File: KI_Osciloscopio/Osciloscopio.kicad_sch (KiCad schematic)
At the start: 40 parts, among them J1 Barrel Jack, U1 MCP6004, U2 74HC4051, U3 LM7805, U4 LM1117-3.3

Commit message: Esquematico terminado
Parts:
- removed U3: LM7805, Package_TO_SOT_THT:TO-220-3_Vertical, symbol Regulator_Linear:LM7805_TO220
- removed V1: VALUE, symbol pspice:VSOURCE
- added CN10: Conn_01x02_Female, symbol Connector:Conn_01x02_Female
- added CN5: Conn_01x10_Male, symbol Connector:Conn_01x10_Male
- added CN6, CN9: Conn_01x08_Male, symbol Connector:Conn_01x08_Male
- added CN8: Conn_01x06_Male, symbol Connector:Conn_01x06_Male
- added J1: Conn_Coaxial, symbol Connector:Conn_Coaxial
- added J2: USB_B, symbol Connector:USB_B
- added J2: OLED 128x64, symbol Connector:Conn_01x04_Male
- added JP1: Jumper_2_Open, symbol Jumper:Jumper_2_Open
- added U3: LM2940CT-5.0/NOPB, TO_SOT_Packages_THT:TO-220_Vertical, symbol AOI-LM2940CT:LM2940CT-5.0/NOPB
- added U5: M95128, Package_SO:SOIC-8_3.9x4.9mm_P1.27mm, symbol Memory_EEPROM:M95256-WMN6P
- C1: value 100uF -> 22uF
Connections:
- net 3.3V: now also CN6.5 (Pin_5), J2.3 (Pin_3), U5.3 (~{W}), U5.7 (~{HOLD}), U5.8 (VCC)
- net A0: now also CN8.1 (Pin_1)
- net A1: now also CN8.2 (Pin_2)
- net Earth: now also U3.2 (GND)
- net GNDREF: now also CN5.7 (Pin_7), CN6.2 (Pin_2), CN6.3 (Pin_3), J1.2 (Ext), J2.4 (GND), J2.4 (Pin_4), J2.5 (Shield), U5.4 (VSS)
- net VCC: now also CN6.4 (Pin_4), JP1.1 (A), U3.3 (OUT)
- net VDD: now also U3.1 (IN)
- net at C1.2: now also J1.1 (In)
- net D06 renamed D9
- net D9: now also CN5.2 (Pin_2)
- net D09 renamed D6
- net D6: now also CN9.7 (Pin_7)
- net D11 renamed D8
- net D8: now also CN5.1 (Pin_1)
- net D12 renamed D7
- net D7: now also CN9.8 (Pin_8)
- new net A2: CN8.3 (Pin_3)
- new net A3: CN8.4 (Pin_4)
- new net A4: CN8.5 (Pin_5)
- new net A5: CN8.6 (Pin_6)
- new net AVDD: CN5.8 (Pin_8)
- new net CS: CN5.3 (Pin_3), U5.1 (~{S})
- new net D+: CN10.1 (Pin_1), J2.3 (D+)
- new net D-: CN10.2 (Pin_2), J2.2 (D-)
- new net D0: CN9.1 (Pin_1)
- new net D1: CN9.2 (Pin_2)
- new net D2: CN9.3 (Pin_3)
- new net D3: CN9.4 (Pin_4)
- new net D4: CN9.5 (Pin_5)
- new net D5: CN9.6 (Pin_6)
- new net IOREF: CN6.7 (Pin_7)
- new net MISO: CN5.5 (Pin_5), U5.2 (Q)
- new net MOSI: CN5.4 (Pin_4), U5.5 (D)
- new net NRST: CN6.6 (Pin_6)
- new net SCK: CN5.6 (Pin_6), U5.6 (C)
- new net SCL: CN5.10 (Pin_10), J2.2 (Pin_2)
- new net SDA: CN5.9 (Pin_9), J2.1 (Pin_1)
- new net VBUS: J2.1 (VBUS)
- new net VIN: CN6.1 (Pin_1), JP1.2 (B)
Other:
- note added: "ALIMENTACION"
- note added: "STM32F401RE"
- moved on the sheet: C1, C11, C12, C2, C3, C4, C5, C6, C7, C8, C9, D3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

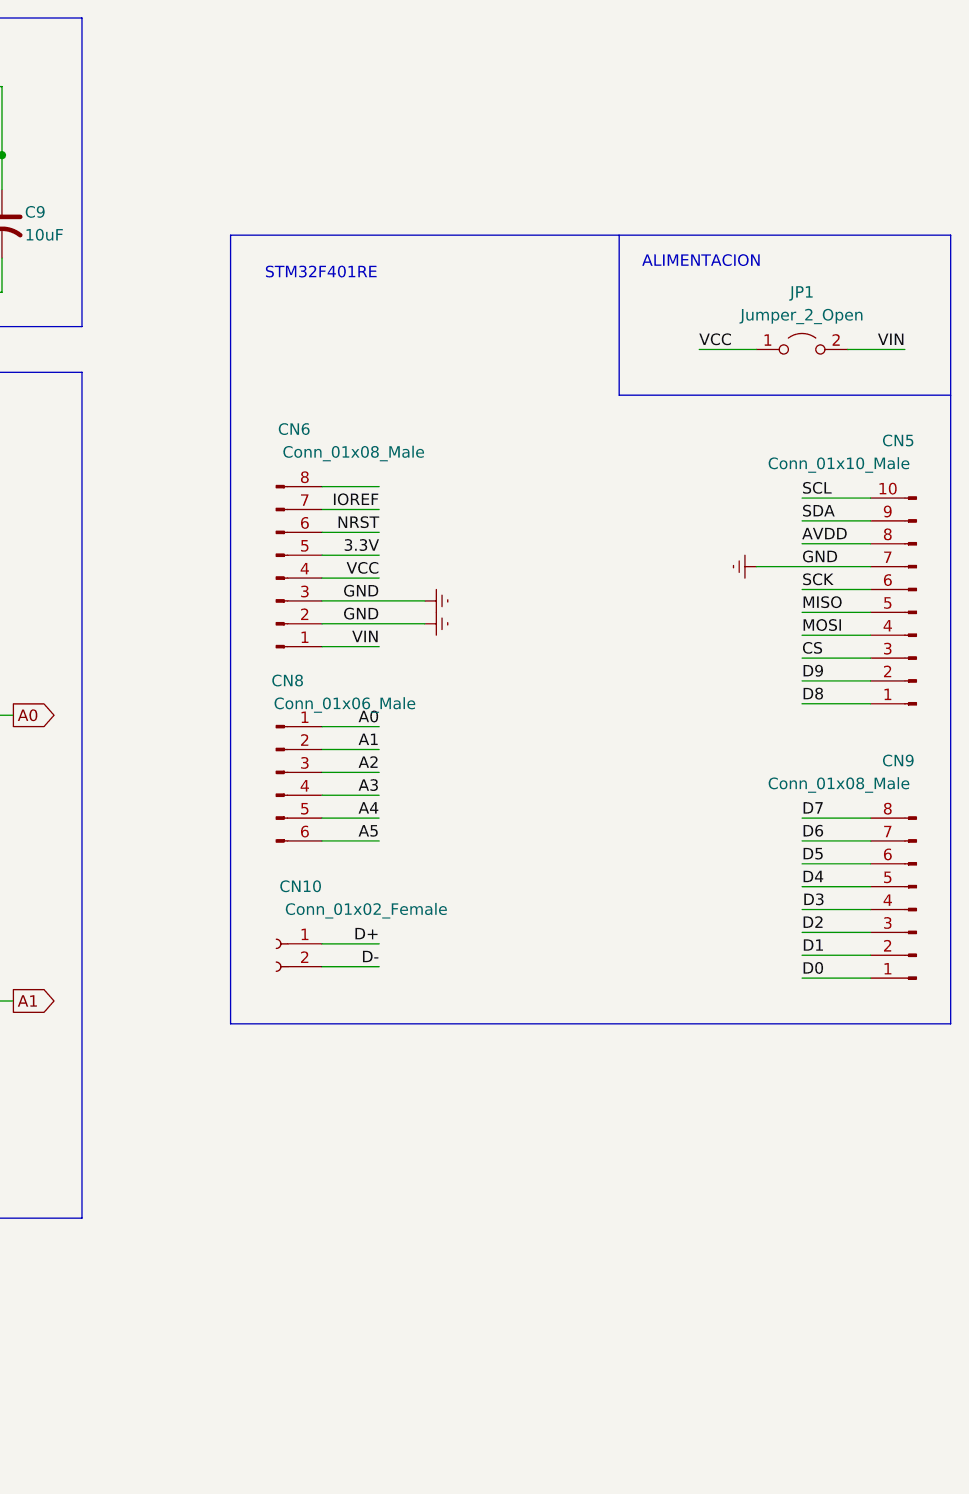
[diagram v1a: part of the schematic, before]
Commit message: Agregue Pines para ST en la placa
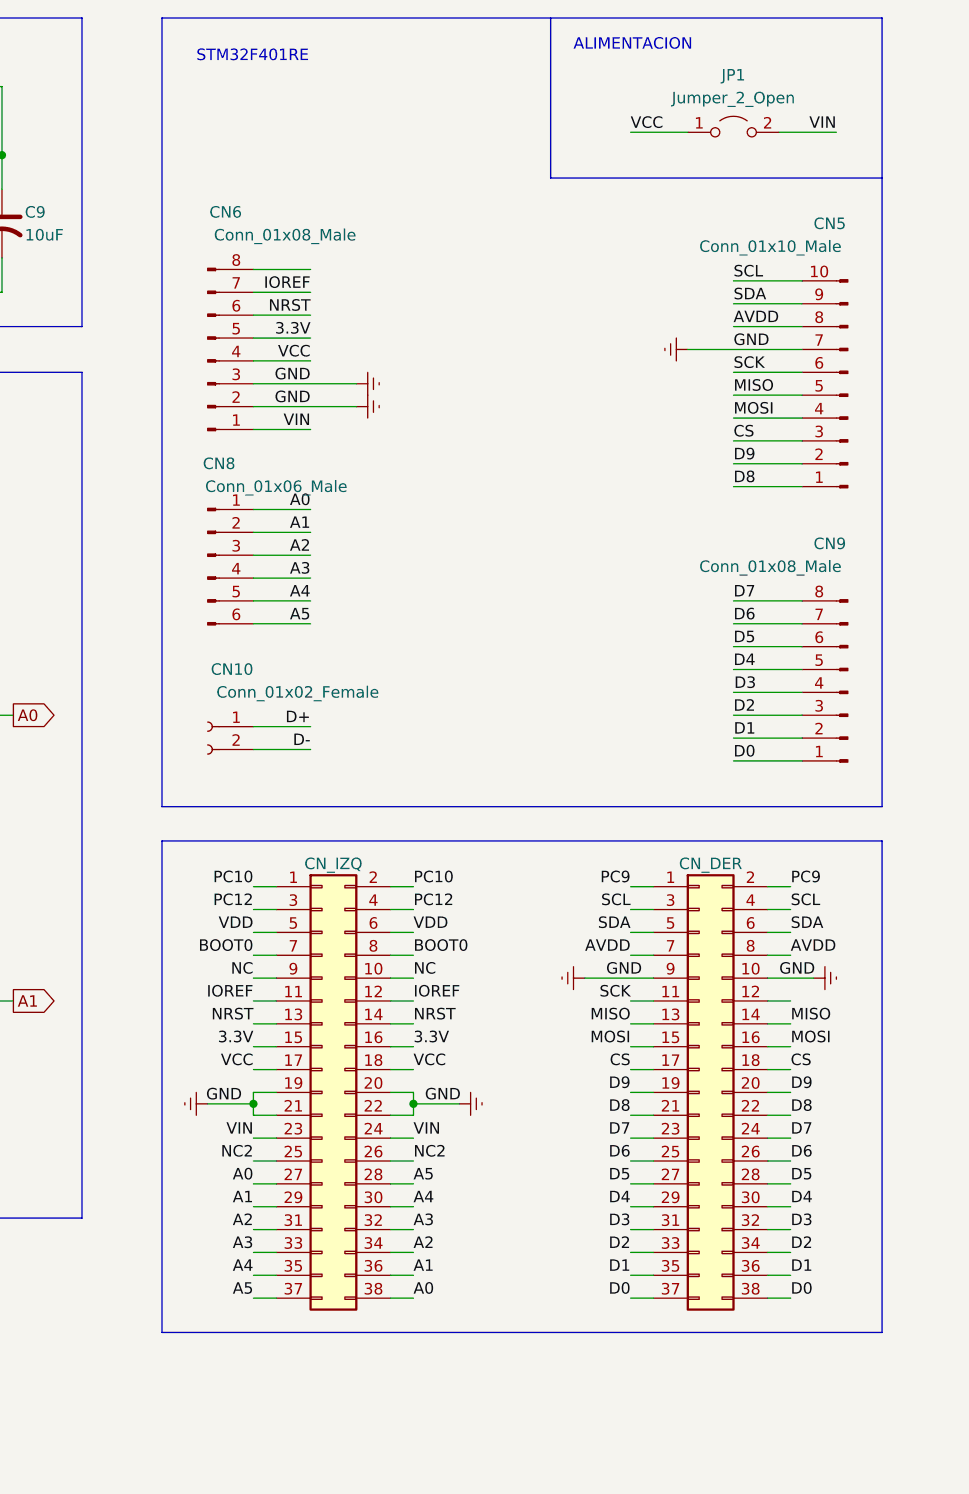
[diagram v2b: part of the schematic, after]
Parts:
- added CN_DER, CN_IZQ: Conn_02x19_Odd_Even, symbol Connector_Generic:Conn_02x19_Odd_Even
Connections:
- net GNDREF is gone; now on net Earth: C11.1, CN5.7 (Pin_7), CN6.2 (Pin_2), CN6.3 (Pin_3), J1.2 (Ext), J2.4 (GND), J2.4 (Pin_4), J2.5 (Shield), R12.2, R17.2, R20.2, U2.7 (VEE), U2.8 (GND), U5.4 (VSS)
- net 3.3V: now also CN_IZQ.15 (Pin_15), CN_IZQ.16 (Pin_16)
- net A0: now also CN_IZQ.27 (Pin_27), CN_IZQ.38 (Pin_38)
- net A1: now also CN_IZQ.29 (Pin_29), CN_IZQ.36 (Pin_36)
- net A2: now also CN_IZQ.31 (Pin_31), CN_IZQ.34 (Pin_34)
- net A3: now also CN_IZQ.32 (Pin_32), CN_IZQ.33 (Pin_33)
- net A4: now also CN_IZQ.30 (Pin_30), CN_IZQ.35 (Pin_35)
- net A5: now also CN_IZQ.28 (Pin_28), CN_IZQ.37 (Pin_37)
- net AVDD: now also CN_DER.7 (Pin_7), CN_DER.8 (Pin_8)
- net CS: now also CN_DER.17 (Pin_17), CN_DER.18 (Pin_18)
- net D0: now also CN_DER.37 (Pin_37), CN_DER.38 (Pin_38)
- net D1: now also CN_DER.35 (Pin_35), CN_DER.36 (Pin_36)
- net D2: now also CN_DER.33 (Pin_33), CN_DER.34 (Pin_34)
- net D3: now also CN_DER.31 (Pin_31), CN_DER.32 (Pin_32)
- net D4: now also CN_DER.29 (Pin_29), CN_DER.30 (Pin_30)
- net D5: now also CN_DER.27 (Pin_27), CN_DER.28 (Pin_28)
- net D6: now also CN_DER.25 (Pin_25), CN_DER.26 (Pin_26)
- net D7: now also CN_DER.23 (Pin_23), CN_DER.24 (Pin_24)
- net D8: now also CN_DER.21 (Pin_21), CN_DER.22 (Pin_22)
- net D9: now also CN_DER.19 (Pin_19), CN_DER.20 (Pin_20)
- net Earth: now also CN_DER.10 (Pin_10), CN_DER.9 (Pin_9), CN_IZQ.19 (Pin_19), CN_IZQ.20 (Pin_20), CN_IZQ.21 (Pin_21), CN_IZQ.22 (Pin_22)
- net IOREF: now also CN_IZQ.11 (Pin_11), CN_IZQ.12 (Pin_12)
- net MISO: now also CN_DER.13 (Pin_13), CN_DER.14 (Pin_14)
- net MOSI: now also CN_DER.15 (Pin_15), CN_DER.16 (Pin_16)
- net NRST: now also CN_IZQ.13 (Pin_13), CN_IZQ.14 (Pin_14)
- net SCK: now also CN_DER.11 (Pin_11)
- net SCL: now also CN_DER.3 (Pin_3), CN_DER.4 (Pin_4)
- net SDA: now also CN_DER.5 (Pin_5), CN_DER.6 (Pin_6)
- net VCC: now also CN_IZQ.17 (Pin_17), CN_IZQ.18 (Pin_18)
- net VDD: now also CN_IZQ.5 (Pin_5), CN_IZQ.6 (Pin_6)
- net VIN: now also CN_IZQ.23 (Pin_23), CN_IZQ.24 (Pin_24)
- new net BOOT0: CN_IZQ.7 (Pin_7), CN_IZQ.8 (Pin_8)
- new net NC: CN_IZQ.10 (Pin_10), CN_IZQ.9 (Pin_9)
- new net NC2: CN_IZQ.25 (Pin_25), CN_IZQ.26 (Pin_26)
- new net PC10: CN_IZQ.1 (Pin_1), CN_IZQ.2 (Pin_2)
- new net PC12: CN_IZQ.3 (Pin_3), CN_IZQ.4 (Pin_4)
- new net PC9: CN_DER.1 (Pin_1), CN_DER.2 (Pin_2)
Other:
- moved on the sheet: CN10, CN5, CN6, CN8, CN9, JP1

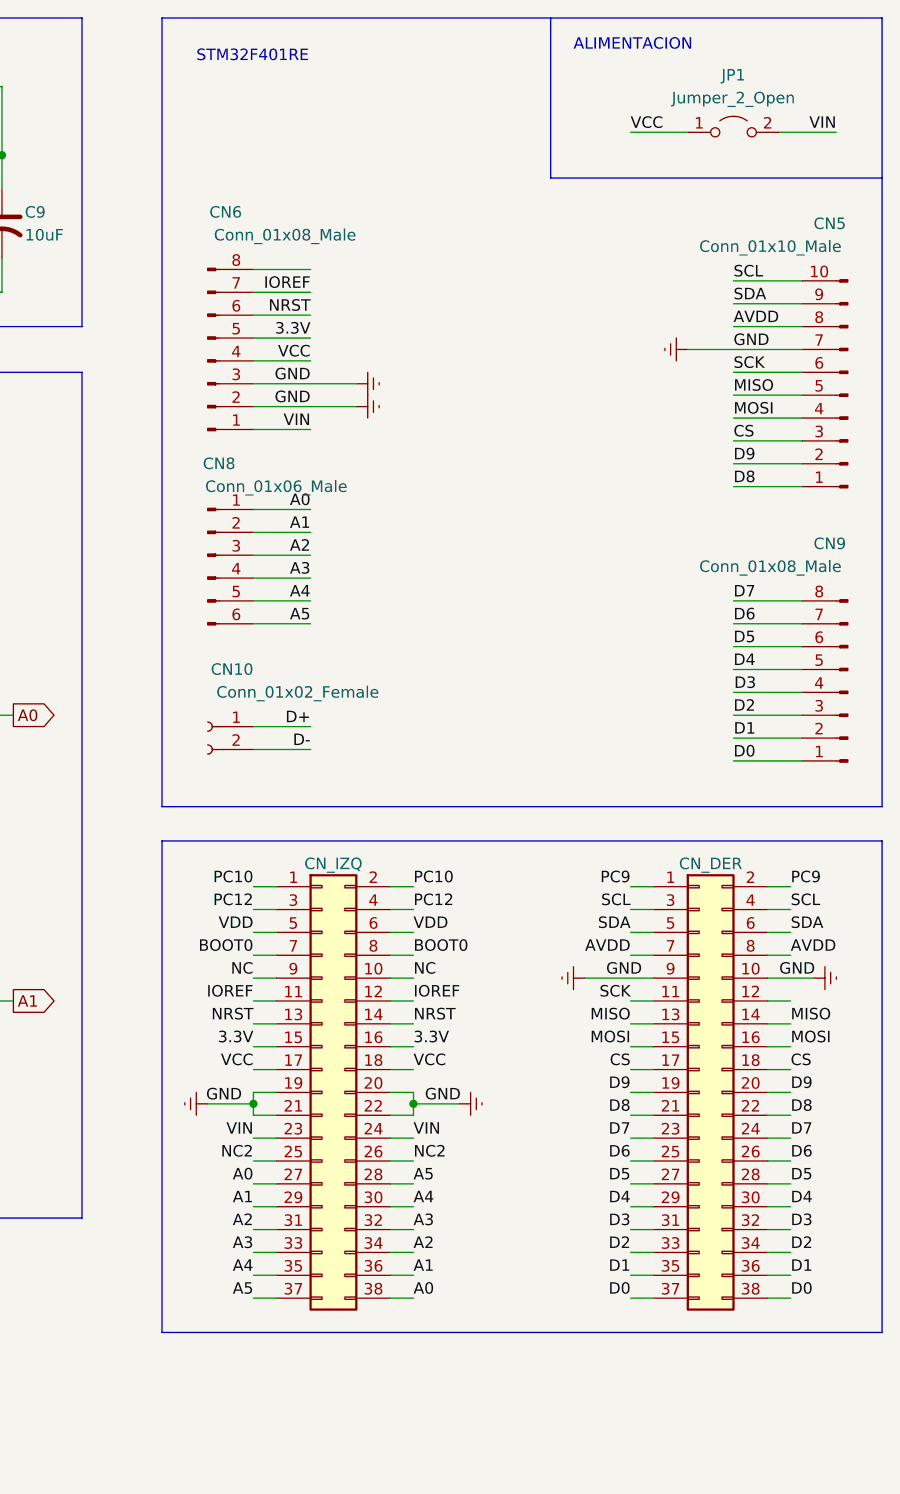
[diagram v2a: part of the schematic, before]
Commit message: Agregue algunos footprints
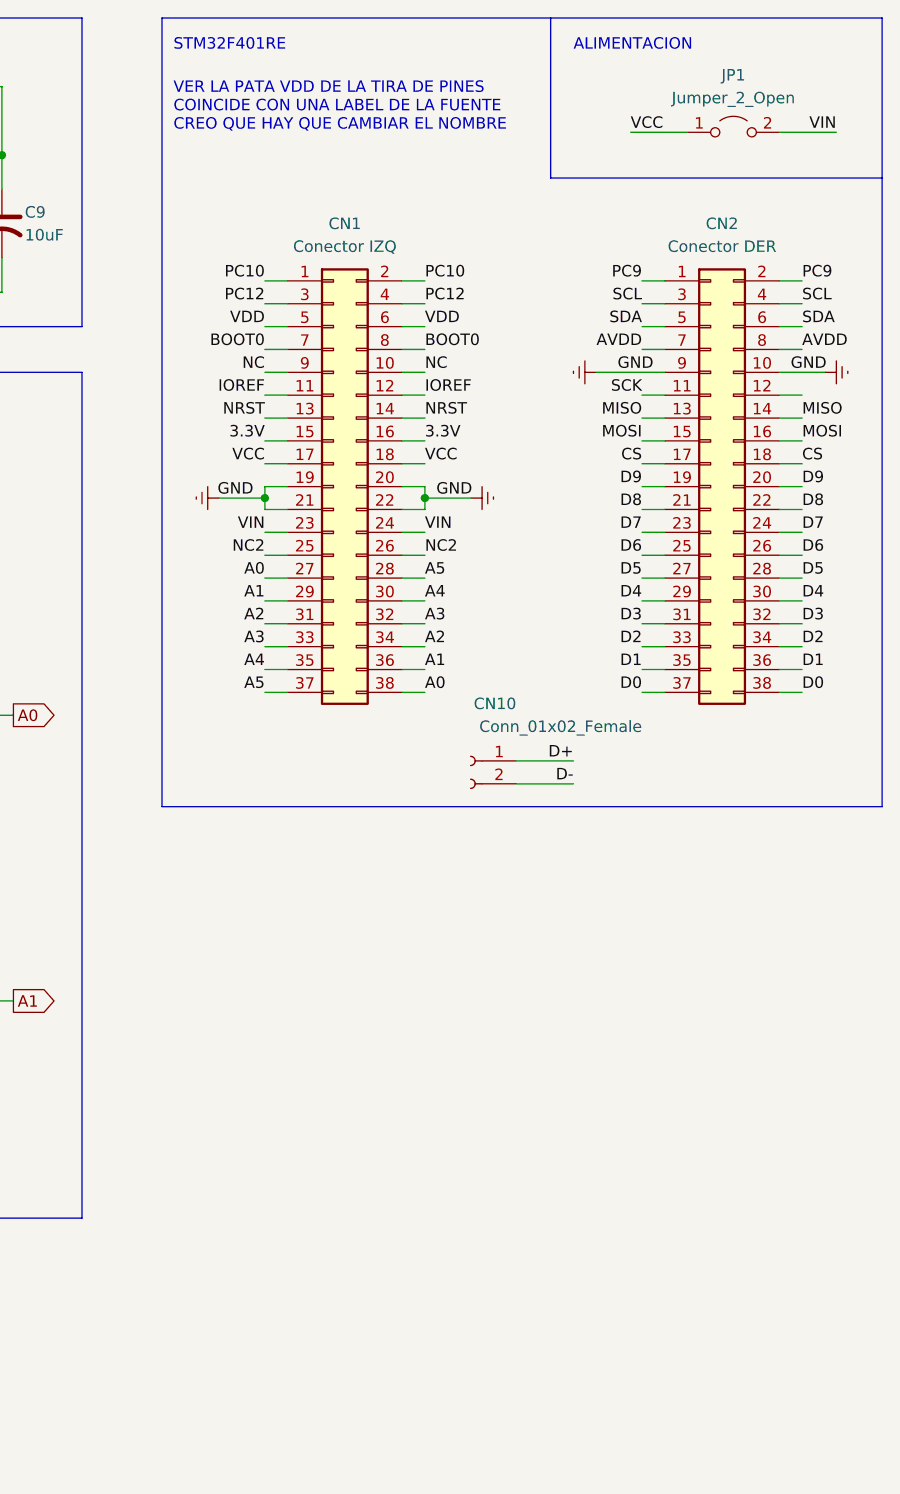
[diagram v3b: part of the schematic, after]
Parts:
- removed CN5: Conn_01x10_Male, symbol Connector:Conn_01x10_Male
- removed CN6, CN9: Conn_01x08_Male, symbol Connector:Conn_01x08_Male
- removed CN8: Conn_01x06_Male, symbol Connector:Conn_01x06_Male
- removed CN_DER, CN_IZQ: Conn_02x19_Odd_Even, symbol Connector_Generic:Conn_02x19_Odd_Even
- added CN1: Conector IZQ, Connector_PinSocket_2.54mm:PinSocket_2x19_P2.54mm_Vertical, symbol Connector_Generic:Conn_02x19_Odd_Even
- added CN2: Conector DER, Connector_PinSocket_2.54mm:PinSocket_2x19_P2.54mm_Vertical, symbol Connector_Generic:Conn_02x19_Odd_Even
- C1, C6, C9: footprint (none) -> Capacitor_THT:C_Radial_D6.3mm_H11.0mm_P2.50mm
- R1, R10, R11, R12, R13, R14, R15, R16, R17, R18, R19, R2, R20, R3, R4, R5, R6, R7, R9: footprint (none) -> Resistor_THT:R_Axial_DIN0207_L6.3mm_D2.5mm_P7.62mm_Horizontal
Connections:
- net 3.3V: now also CN1.15 (Pin_15), CN1.16 (Pin_16)
- net A0: now also CN1.27 (Pin_27), CN1.38 (Pin_38)
- net A1: now also CN1.29 (Pin_29), CN1.36 (Pin_36)
- net A2: now also CN1.31 (Pin_31), CN1.34 (Pin_34)
- net A3: now also CN1.32 (Pin_32), CN1.33 (Pin_33)
- net A4: now also CN1.30 (Pin_30), CN1.35 (Pin_35)
- net A5: now also CN1.28 (Pin_28), CN1.37 (Pin_37)
- net AVDD: now also CN2.7 (Pin_7), CN2.8 (Pin_8)
- net BOOT0: now also CN1.7 (Pin_7), CN1.8 (Pin_8)
- net CS: now also CN2.17 (Pin_17), CN2.18 (Pin_18)
- net D0: now also CN2.37 (Pin_37), CN2.38 (Pin_38)
- net D1: now also CN2.35 (Pin_35), CN2.36 (Pin_36)
- net D2: now also CN2.33 (Pin_33), CN2.34 (Pin_34)
- net D3: now also CN2.31 (Pin_31), CN2.32 (Pin_32)
- net D4: now also CN2.29 (Pin_29), CN2.30 (Pin_30)
- net D5: now also CN2.27 (Pin_27), CN2.28 (Pin_28)
- net D6: now also CN2.25 (Pin_25), CN2.26 (Pin_26)
- net D7: now also CN2.23 (Pin_23), CN2.24 (Pin_24)
- net D8: now also CN2.21 (Pin_21), CN2.22 (Pin_22)
- net D9: now also CN2.19 (Pin_19), CN2.20 (Pin_20)
- net Earth: now also CN1.19 (Pin_19), CN1.20 (Pin_20), CN1.21 (Pin_21), CN1.22 (Pin_22), CN2.10 (Pin_10), CN2.9 (Pin_9)
- net IOREF: now also CN1.11 (Pin_11), CN1.12 (Pin_12)
- net MISO: now also CN2.13 (Pin_13), CN2.14 (Pin_14)
- net MOSI: now also CN2.15 (Pin_15), CN2.16 (Pin_16)
- net NC: now also CN1.10 (Pin_10), CN1.9 (Pin_9)
- net NC2: now also CN1.25 (Pin_25), CN1.26 (Pin_26)
- net NRST: now also CN1.13 (Pin_13), CN1.14 (Pin_14)
- net PC10: now also CN1.1 (Pin_1), CN1.2 (Pin_2)
- net PC12: now also CN1.3 (Pin_3), CN1.4 (Pin_4)
- net PC9: now also CN2.1 (Pin_1), CN2.2 (Pin_2)
- net SCK: now also CN2.11 (Pin_11)
- net SCL: now also CN2.3 (Pin_3), CN2.4 (Pin_4)
- net SDA: now also CN2.5 (Pin_5), CN2.6 (Pin_6)
- net VCC: now also CN1.17 (Pin_17), CN1.18 (Pin_18)
- net VDD: now also CN1.5 (Pin_5), CN1.6 (Pin_6)
- net VIN: now also CN1.23 (Pin_23), CN1.24 (Pin_24)
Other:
- note added: "VER LA PATA VDD DE LA TIRA DE PINES COINCIDE CON UNA LABEL DE LA FUENTE CREO QUE HAY QUE CAMBIAR EL NOMBRE"
- moved on the sheet: CN10

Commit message: Complete la BOM con los footprints
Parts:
- removed CN10: Conn_01x02_Female, symbol Connector:Conn_01x02_Female
- C11, C12, C2, C3, C4, C5, C7, C8: footprint (none) -> Capacitor_THT:C_Disc_D5.0mm_W2.5mm_P2.50mm
- D4: footprint (none) -> Diode_THT:D_DO-15_P10.16mm_Horizontal
- J1: footprint (none) -> Connector_BarrelJack:BarrelJack_Horizontal
- J2: renamed from J1; footprint (none) -> Connector_Coaxial:BNC_Amphenol_B6252HB-NPP3G-50_Horizontal
- J4: renamed from J2; footprint (none) -> Connector_USB:USB_B_Amphenol_MUSB-D511_Vertical_Rugged
- U2: footprint (none) -> Package_DIP:DIP-16_W7.62mm
- U3: footprint TO_SOT_Packages_THT:TO-220_Vertical -> Package_TO_SOT_THT:TO-220-3_Vertical
- U4: footprint (none) -> Package_TO_SOT_THT:TO-220-3_Vertical
- U5: footprint Package_SO:SOIC-8_3.9x4.9mm_P1.27mm -> Package_DIP:DIP-8_W7.62mm
- renumbered J2 to J3
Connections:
- net SCK: now also CN2.12 (Pin_12)
- net VDD: no longer CN1.6 (Pin_6)
- new net VDDD: CN1.6 (Pin_6)
